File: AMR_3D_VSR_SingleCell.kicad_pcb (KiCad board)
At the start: 2 copper layers, 270.1 x 125 mm, 85 parts, among them P1 CONN_01X01, P2 CONN_01X01, P3 CONN_02X15, P4 CONN_02X05, P5 CONN_02X02, U1 AFF755b, U10 AFF755b, U11 AFF755b, U12 AFF755b, U13 AFF755b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

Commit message: New PCB Layout included, Routing of the signal channesl done.  Committer: Schmitz <ltu@basisit.de>  Changes to be committed: 	modified:   AMR_3D_VSR_SingleCell.kicad_pcb 	modified:   AMR_3D_VSR_SingleCell.kicad_pcb-bak 	modified:   drawing2.dxf
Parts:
- removed the REF** at (144.7, 126.7)
- removed the REF** at (273.7, 145.1)
- moved REF** 338.4 mm to (68.6, -115.7)
- moved REF** 329.0 mm to (80.5, -113.9)
- moved REF** 328.7 mm to (178.2, -113.5)
- moved REF** 324.5 mm to (90.2, -116.8)
- moved REF** 322.2 mm to (123.0, -112.0)
- moved REF** 321.7 mm to (106.7, -119.9)
- moved REF** 317.7 mm to (145.7, -108.9)
- moved REF** 316.1 mm to (126.4, -121.4)
- moved REF** 314.3 mm to (135.2, -119.6)
- moved REF** 314.2 mm to (118.9, -118.8)
- moved REF** 313.8 mm to (152.7, -117.4)
- moved REF** 307.3 mm to (167.5, -111.8)
- moved REF** 296.1 mm to (267.8, -163.1)
- moved REF** 276.5 mm to (277.7, -186.0)
- moved REF** 275.4 mm to (270.2, -176.8)
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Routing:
- net LP-: track 1270.5 -> 0.00 mm, vias 35 -> 0
- net LP+: track 476.5 -> 0.00 mm, vias 19 -> 0
- net +12V: track 148.1 -> 0.00 mm
- net +6V: track 147.6 -> 0.00 mm, vias 6 -> 0
- net U12-: track 120.9 -> 66.0 mm
- net U12+: track 109.8 -> 55.5 mm
- net U15+: track 138.6 -> 85.3 mm
- net Net-(U10-Pad3): track 52.7 -> 0.00 mm
- net Net-(U10-Pad1): track 52.7 -> 0.00 mm
- net U15-: track 145.2 -> 95.4 mm
- net Net-(U5-Pad8): track 45.9 -> 0.00 mm
- net Net-(U5-Pad7): track 40.9 -> 0.00 mm
- net U14+: track 134.9 -> 94.7 mm
- net U14-: track 141.7 -> 105.0 mm
- net Net-(U10-Pad7): track 33.7 -> 0.00 mm, vias 2 -> 0
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- removed copper zone on B.Cu, net LP2-
- removed copper zone on F.Cu, net LP2-
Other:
- board size 270.1 x 125 mm -> 200.8 x 132.1 mm

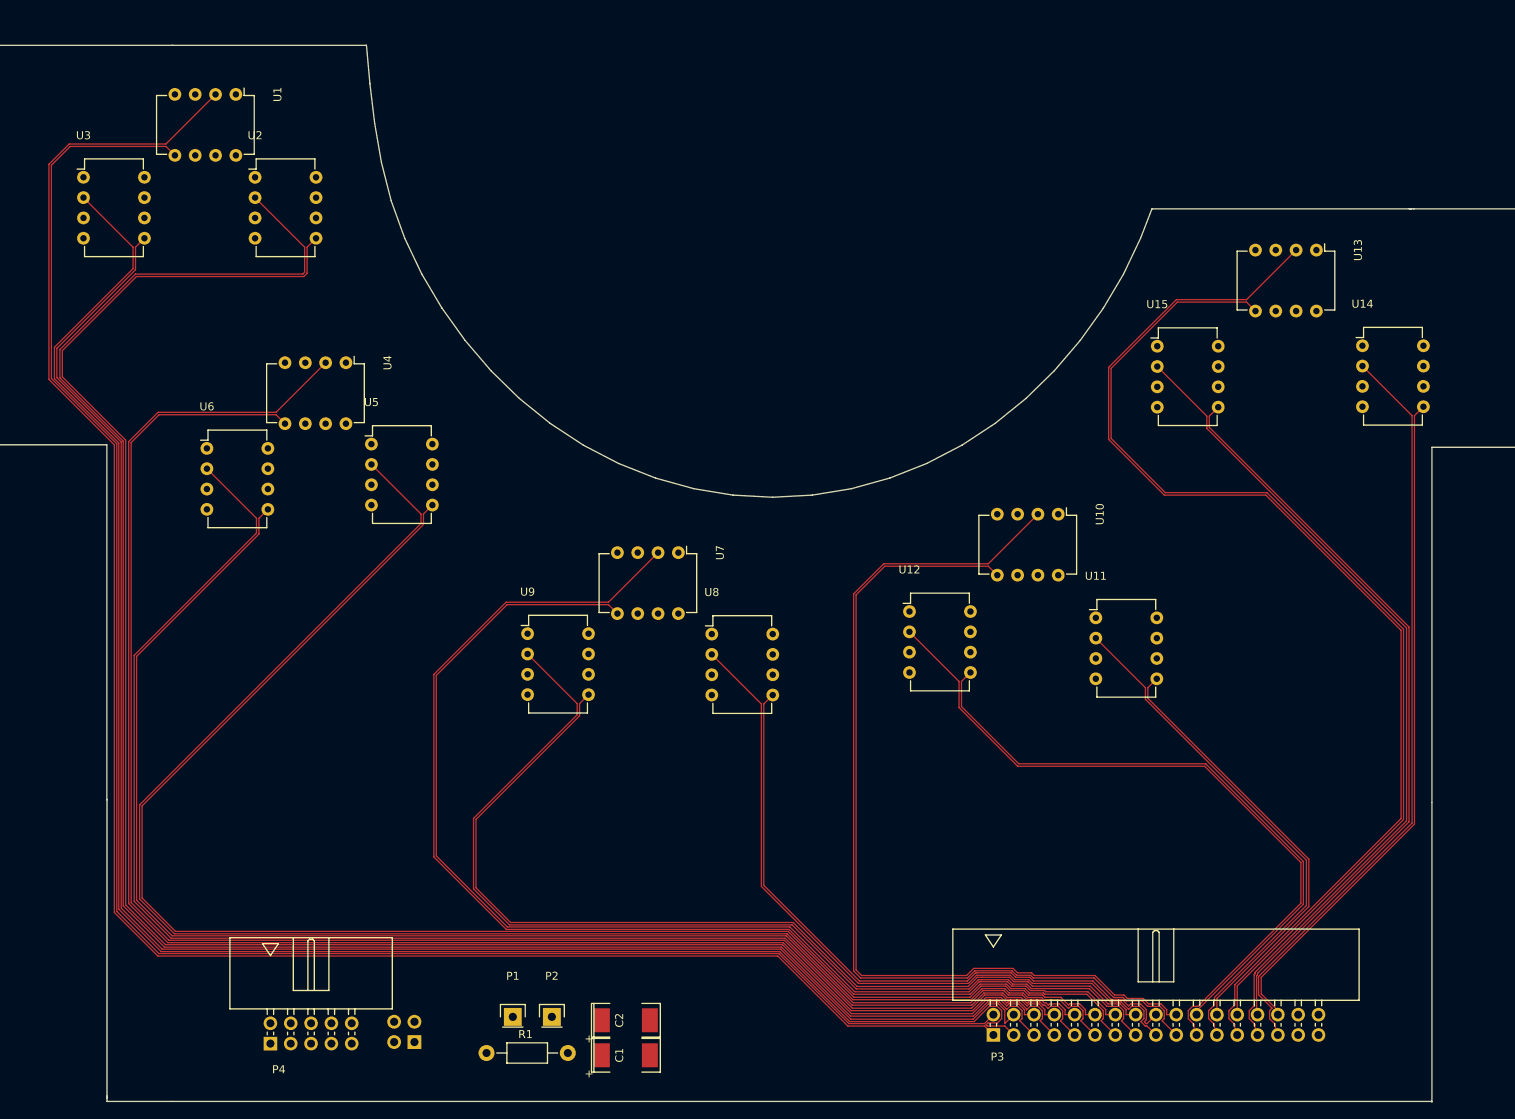
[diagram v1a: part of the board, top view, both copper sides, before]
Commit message: Testspulen verdrahtet.  Committer: Schmitz <ltu@basisit.de>  Changes to be committed: 	modified:   AMR_3D_VSR_SingleCell.kicad_pcb 	modified:   AMR_3D_VSR_SingleCell.kicad_pcb-bak
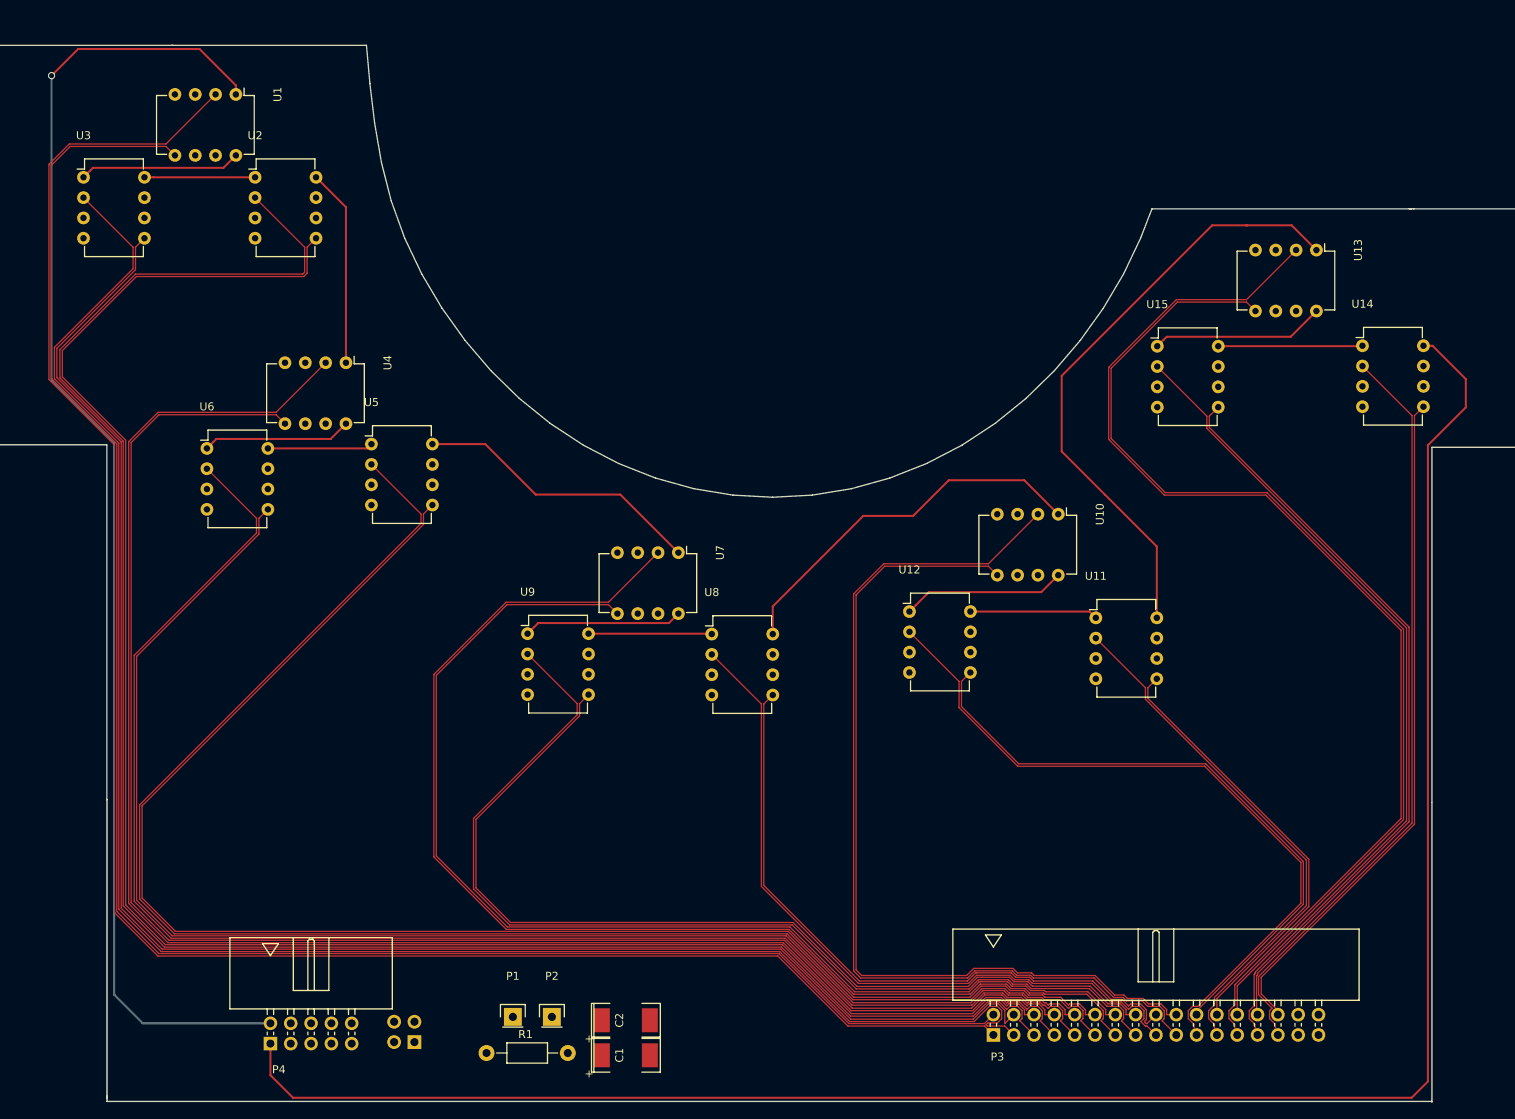
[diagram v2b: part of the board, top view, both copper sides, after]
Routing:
- net LP-: track 0.00 -> 247.4 mm
- net +12V: track 0.00 -> 166.6 mm, vias 0 -> 1
- net Net-(U11-Pad8): track 0.00 -> 76.3 mm
- net Net-(U10-Pad1): track 0.00 -> 47.4 mm
- net Net-(U5-Pad8): track 0.00 -> 36.4 mm
- net Net-(U2-Pad8): track 0.00 -> 24.7 mm
- net Net-(U13-Pad8): track 0.00 -> 21.7 mm
- net Net-(U10-Pad8): track 0.00 -> 20.5 mm
- net Net-(U1-Pad8): track 0.00 -> 20.2 mm
- net Net-(U7-Pad8): track 0.00 -> 19.9 mm
- net Net-(U4-Pad8): track 0.00 -> 18.7 mm
- net Net-(U14-Pad1): track 0.00 -> 18.1 mm
- net Net-(U11-Pad1): track 0.00 -> 16.0 mm
- net Net-(U8-Pad1): track 0.00 -> 15.4 mm
- net Net-(U2-Pad1): track 0.00 -> 13.8 mm
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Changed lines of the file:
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@@
     (thickness 1.6)
     (drawings 58)
-    (tracks 504)
+    (tracks 576)
     (zones 0)
     (modules 83)
@@
     (arrow2b (pts (xy 210.010183 210.239955) (xy 209.42319 209.11375)))
   )
+  (segment (start 131.69222 203.21076) (end 131.69298 203.21) (width 0.254) (layer B.Cu) (net 2))
+  (segment (start 131.69298 203.21) (end 147.65 203.21) (width 0.254) (layer B.Cu) (net 2))
+  (segment (start 128.12606 199.6446) (end 131.69222 203.21076) (width 0.254) (layer B.Cu) (net 2))
+  (segment (start 128.12606 130.71916) (end 128.12606 199.6446) (width 0.254) (layer B.Cu) (net 2))
+  (segment (start 120.29016 122.88326) (end 128.12606 130.71916) (width 0.254) (layer B.Cu) (net 2))
+  (segment (start 120.29016 84.75024) (end 120.29016 122.88326) (width 0.254) (layer B.Cu) (net 2))
+  (segment (start 138.78675 81.42538) (end 123.61502 81.42538) (width 0.254) (layer F.Cu) (net 2))
+  (segment (start 123.61502 81.42538) (end 120.29016 84.75024) (width 0.254) (layer F.Cu) (net 2))
+  (via (at 120.29016 84.75024) (size 0.889) (drill 0.635) (layers F.Cu B.Cu) (net 2))
+  (segment (start 143.33 87.1) (end 143.33 85.96863) (width 0.254) (layer F.Cu) (net 2))
+  (segment (start 143.33 85.96863) (end 138.78675 81.42538) (width 0.254) (layer F.Cu) (net 2))
+  (segment (start 143.33 94.72) (end 141.771001 96.278999) (width 0.254) (layer F.Cu) (net 5))
+  (segment (start 141.771001 96.278999) (end 125.461001 96.278999) (width 0.254) (layer F.Cu) (net 5))
+  (segment (start 125.461001 96.278999) (end 125.079999 96.660001) (width 0.254) (layer F.Cu) (net 5))
+  (segment (start 125.079999 96.660001) (end 124.28 97.46) (width 0.254) (layer F.Cu) (net 5))
+  (segment (start 153.35 97.46) (end 157.09 101.2) (width 0.254) (layer F.Cu) (net 7))
+  (segment (start 157.09 101.2) (end 157.09 120.64) (width 0.254) (layer F.Cu) (net 7))
+  (segment (start 157.09 128.26) (end 155.181001 130.168999) (width 0.254) (layer F.Cu) (net 9))
+  (segment (start 155.181001 130.168999) (end 140.891001 130.168999) (width 0.254) (layer F.Cu) (net 9))
+  (segment (start 140.891001 130.168999) (end 140.509999 130.550001) (width 0.254) (layer F.Cu) (net 9))
+  (segment (start 140.509999 130.550001) (end 139.71 131.35) (width 0.254) (layer F.Cu) (net 9))
+  (segment (start 180.81328 137.11996) (end 191.38396 137.11996) (width 0.254) (layer F.Cu) (net 11))
+  (segment (start 191.38396 137.11996) (end 198.643 144.379) (width 0.254) (layer F.Cu) (net 11))
+  (segment (start 174.50392 130.8106) (end 180.81328 137.11996) (width 0.254) (layer F.Cu) (net 11))
+  (segment (start 167.89484 130.8106) (end 174.50392 130.8106) (width 0.254) (layer F.Cu) (net 11))
+  (segment (start 198.643 151.999) (end 197.461999 153.180001) (width 0.254) (layer F.Cu) (net 13))
+  (segment (start 197.461999 153.180001) (end 181.121999 153.180001) (width 0.254) (layer F.Cu) (net 13))
+  (segment (start 181.121999 153.180001) (end 180.592999 153.709001) (width 0.254) (layer F.Cu) (net 13))
+  (segment (start 180.592999 153.709001) (end 179.793 154.509) (width 0.254) (layer F.Cu) (net 13))
+  (segment (start 232.44132 135.32926) (end 241.8825 135.32926) (width 0.254) (layer F.Cu) (net 15))
+  (segment (start 241.8825 135.32926) (end 246.12684 139.5736) (width 0.254) (layer F.Cu) (net 15))
+  (segment (start 227.98616 139.78442) (end 232.44132 135.32926) (width 0.254) (layer F.Cu) (net 15))
+  (segment (start 221.75808 139.78442) (end 227.98616 139.78442) (width 0.254) (layer F.Cu) (net 15))
+  (segment (start 210.43984 151.10266) (end 221.75808 139.78442) (width 0.254) (layer F.Cu) (net 15))
+  (segment (start 210.43984 154.5596) (end 210.43984 151.10266) (width 0.254) (layer F.Cu) (net 15))
+  (segment (start 246.12684 147.1936) (end 244.00594 149.3145) (width 0.254) (layer F.Cu) (net 17))
+  (segment (start 244.00594 149.3145) (end 229.95466 149.3145) (width 0.254) (layer F.Cu) (net 17))
+  (segment (start 229.95466 149.3145) (end 228.328959 150.940201) (width 0.254) (layer F.Cu) (net 17))
+  (segment (start 228.328959 150.940201) (end 227.52896 151.7402) (width 0.254) (layer F.Cu) (net 17))
+  (segment (start 269.558738 103.46242) (end 269.759 103.46242) (width 0.254) (layer F.Cu) (net 19))
+  (segment (start 269.759 103.46242) (end 275.30128 103.46242) (width 0.254) (layer F.Cu) (net 19))
+  (segment (start 246.5561 122.27874) (end 265.37242 103.46242) (width 0.254) (layer F.Cu) (net 19))
+  (segment (start 265.37242 103.46242) (end 269.759 103.46242) (width 0.254) (layer F.Cu) (net 19))
+  (segment (start 246.5561 131.72246) (end 246.5561 122.27874) (width 0.254) (layer F.Cu) (net 19))
+  (segment (start 251.98497 137.15133) (end 246.5561 131.72246) (width 0.254) (layer F.Cu) (net 19))
+  (segment (start 251.98751 137.15133) (end 251.98497 137.15133) (width 0.254) (layer F.Cu) (net 19))
+  (segment (start 258.44584 152.5276) (end 258.44584 143.60966) (width 0.254) (layer F.Cu) (net 19))
+  (segment (start 258.44584 143.60966) (end 251.98751 137.15133) (width 0.254) (layer F.Cu) (net 19))
+  (segment (start 275.30128 103.46242) (end 278.39754 106.55868) (width 0.254) (layer F.Cu) (net 19))
+  (segment (start 278.39754 114.17868) (end 275.184341 117.391879) (width 0.254) (layer F.Cu) (net 21))
+  (segment (start 275.184341 117.391879) (end 259.685261 117.391879) (width 0.254) (layer F.Cu) (net 21))
+  (segment (start 259.685261 117.391879) (end 259.304259 117.772881) (width 0.254) (layer F.Cu) (net 21))
+  (segment (start 259.304259 117.772881) (end 258.50426 118.57288) (width 0.254) (layer F.Cu) (net 21))
+  (segment (start 150.47552 212.51986) (end 147.65 209.69434) (width 0.254) (layer F.Cu) (net 23))
+  (segment (start 147.65 209.69434) (end 147.65 205.75) (width 0.254) (layer F.Cu) (net 23))
+  (segment (start 290.29998 212.51986) (end 150.47552 212.51986) (width 0.254) (layer F.Cu) (net 23))
+  (segment (start 292.33452 210.48532) (end 290.29998 212.51986) (width 0.254) (layer F.Cu) (net 23))
+  (segment (start 292.33452 130.96046) (end 292.33452 210.48532) (width 0.254) (layer F.Cu) (net 23))
+  (segment (start 297.07416 126.22082) (end 292.33452 130.96046) (width 0.254) (layer F.Cu) (net 23))
+  (segment (start 297.07416 122.68661) (end 297.07416 126.22082) (width 0.254) (layer F.Cu) (net 23))
+  (segment (start 291.77318 118.517) (end 292.90455 118.517) (width 0.254) (layer F.Cu) (net 23))
+  (segment (start 292.90455 118.517) (end 297.07416 122.68661) (width 0.254) (layer F.Cu) (net 23))
   (segment (start 284.15318 121.057) (end 290.350681 127.254501) (width 0.125) (layer F.Cu) (net 24))
   (segment (start 273.275 203.360502) (end 273.275 204.365) (width 0.125) (layer F.Cu) (net 24))
@@
   (segment (start 135.71 94.72) (end 134.592499 93.602499) (width 0.125) (layer F.Cu) (net 53))
   (segment (start 134.592499 93.602499) (end 122.626367 93.602499) (width 0.125) (layer F.Cu) (net 53))
+  (segment (start 131.9 97.46) (end 133.03137 97.46) (width 0.254) (layer F.Cu) (net 54))
+  (segment (start 133.03137 97.46) (end 145.73 97.46) (width 0.254) (layer F.Cu) (net 54))
+  (segment (start 147.33 131.35) (end 159.73544 131.35) (width 0.254) (layer F.Cu) (net 56))
+  (segment (start 159.73544 131.35) (end 160.27484 130.8106) (width 0.254) (layer F.Cu) (net 56))
+  (segment (start 187.413 154.509) (end 202.76924 154.509) (width 0.254) (layer F.Cu) (net 58))
+  (segment (start 202.76924 154.509) (end 202.81984 154.5596) (width 0.254) (layer F.Cu) (net 58))
+  (segment (start 235.14896 151.7402) (end 250.03844 151.7402) (width 0.254) (layer F.Cu) (net 60))
+  (segment (start 250.03844 151.7402) (end 250.82584 152.5276) (width 0.254) (layer F.Cu) (net 60))
+  (segment (start 266.12426 118.57288) (end 284.0973 118.57288) (width 0.254) (layer F.Cu) (net 62))
+  (segment (start 284.0973 118.57288) (end 284.15318 118.517) (width 0.254) (layer F.Cu) (net 62))
   (zone (net 0) (net_name "") (layer B.Cu) (hatch full 0.508)
     (connect_pads (clearance 0.508))

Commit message: Filling of the Cu Plane fixed.  Committer: Schmitz <ltu@basisit.de>  Changes to be committed: 	modified:   AMR_3D_VSR_SingleCell.kicad_pcb 	modified:   AMR_3D_VSR_SingleCell.kicad_pcb-bak
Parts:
- removed R1: R, Resistors_ThroughHole:Resistor_Horizontal_RM10mm
- removed the REF** at (80.5, -113.9)
- removed the REF** at (177.7, -77.5)
- removed the REF** at (184.3, -80.6)
- removed the REF** at (241.2, -62.3)
- removed the REF** at (118.9, -118.8)
- removed the REF** at (276.1, -127.8)
- removed the REF** at (271.8, -138.4)
- removed the REF** at (231.4, -72.7)
- removed the REF** at (106.7, -119.9)
- removed the REF** at (232.6, -50.1)
- removed the REF** at (194.3, -29.9)
- removed the REF** at (153.1, -30.4)
- removed the REF** at (234.0, -57.4)
- removed the REF** at (227.5, -61.7)
- removed the REF** at (142.7, -29.5)
- removed the REF** at (165.5, -31.5)
- removed the REF** at (179.5, -91.5)
- removed the REF** at (219.4, -41.3)
- removed the REF** at (178.0, -28.2)
- removed the REF** at (90.2, -116.8)
- removed the REF** at (167.5, -111.8)
- removed the REF** at (185.2, -49.9)
- removed the REF** at (123.0, -112.0)
- removed the REF** at (275.8, -170.2)
- removed the REF** at (178.2, -113.5)
- removed the REF** at (290.2, -179.6)
- removed the REF** at (289.2, -123.4)
- removed the REF** at (277.7, -186.0)
- removed the REF** at (272.6, -155.6)
- removed the REF** at (268.6, -122.4)
- removed the REF** at (271.1, -92.8)
- removed the REF** at (279.7, -117.3)
- removed the REF** at (267.8, -163.1)
- removed the REF** at (273.9, -144.6)
- removed the REF** at (268.8, -129.1)
- removed the REF** at (176.3, -86.0)
- removed the REF** at (145.7, -108.9)
- removed the REF** at (135.2, -119.6)
- removed the REF** at (112.5, -29.5)
- removed the REF** at (120.9, -34.3)
- removed the REF** at (152.7, -117.4)
- removed the REF** at (172.5, -91.1)
- removed the REF** at (126.4, -121.4)
- removed the REF** at (270.2, -176.8)
- removed the REF** at (68.6, -115.7)
- removed the REF** at (241.2, -39.2)
- removed the REF** at (94.6, -33.4)
- removed the REF** at (97.2, -40.0)
- removed the REF** at (253.3, -20.8)
- removed the REF** at (184.6, -86.5)
- removed the REF** at (229.3, -39.6)
- removed the REF** at (221.5, -32.5)
- removed the REF** at (285.5, -147.6)
- removed the REF** at (256.5, -37.9)
- removed the REF** at (282.7, -171.5)
- removed the REF** at (282.7, -158.8)
- removed the REF** at (286.2, -134.8)
- added REF**: through hole, Connect:1pin, F.Cu at (185.0, 158.3)
- added REF**: through hole, Connect:1pin, F.Cu at (144.7, 133.6)
- added REF**: through hole, Connect:1pin, F.Cu at (201.7, 153.0)
- added REF**: through hole, Connect:1pin, F.Cu at (293.1, 106.3)
- added REF**: through hole, Connect:1pin, F.Cu at (295.4, 124.4)
- added REF**: through hole, Connect:1pin, F.Cu at (265.1, 114.7)
- moved REF** 177.6 mm to (129.8, 100.7)
- moved REF** 169.2 mm to (215.3, 144.0)
- moved REF** 150.2 mm to (262.6, 120.7)
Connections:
- P4 pad 3: LP- -> LP2-
- P4 pad 5: LP2- -> LP-
- REF** pad 1: LP2- -> LP- (x3)
- U14 pad 7: LP- -> LP2-
- U2 pad 6: LP -> LP+
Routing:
- net LP+: track 0.00 -> 380.4 mm, vias 0 -> 1
- net LP2-: track 0.00 -> 244.9 mm
- net +6V: track 0.00 -> 170.4 mm, vias 0 -> 1
- net Net-(U11-Pad7): track 0.00 -> 74.4 mm
- net LP-: track 247.4 -> 297.2 mm
- net Net-(U10-Pad3): track 0.00 -> 48.1 mm
- net Net-(U7-Pad7): track 0.00 -> 41.4 mm
- net Net-(U1-Pad7): track 0.00 -> 37.3 mm
- net Net-(U5-Pad7): track 0.00 -> 34.5 mm
- net Net-(U13-Pad7): track 0.00 -> 29.0 mm
- net Net-(U2-Pad7): track 0.00 -> 26.7 mm
- net +9V: track 0.00 -> 26.5 mm
- net Net-(U10-Pad7): track 0.00 -> 25.7 mm
- net Net-(U4-Pad7): track 0.00 -> 23.9 mm
- net Net-(U14-Pad3): track 0.00 -> 20.7 mm
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- added copper zone on B.Cu, net LP-
- added copper zone on F.Cu, net LP-

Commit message: HZB Logo added to library and to the PCB.  Committer: Schmitz <ltu@basisit.de>  Changes to be committed: 	modified:   AMR_3D_VSR_SingleCell.kicad_pcb 	modified:   AMR_3D_VSR_SingleCell.kicad_pcb-bak 	modified:   AMR_3D_VSR_SingleCell.pro
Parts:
- added G***: LOGO, hzblogo:logo, F.Cu at (283.8, 167.1)
- moved REF** 82.1 mm to (123.5, 128.1)
- moved REF** 8.43 mm to (207.0, 142.4)
- moved REF** 1.08 mm to (143.6, 133.8)
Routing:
- net Net-(U7-Pad7): track 41.4 -> 29.9 mm
- net Net-(U1-Pad7): track 37.3 -> 29.0 mm
- net Net-(U5-Pad1): track 13.2 -> 20.3 mm
- net Net-(U8-Pad1): track 15.4 -> 22.1 mm
- net Net-(U14-Pad1): track 18.1 -> 24.4 mm
- net +12V: track 167.2 -> 171.5 mm
- net +6V: track 170.4 -> 174.6 mm
- net Net-(U1-Pad8): track 20.2 -> 23.0 mm
- net Net-(U5-Pad8): track 36.4 -> 38.5 mm
- net Net-(U2-Pad1): track 13.8 -> 15.5 mm
- net Net-(U14-Pad3): track 20.7 -> 19.1 mm
- net Net-(U13-Pad7): track 29.0 -> 27.4 mm
- net Net-(U10-Pad3): track 48.1 -> 49.4 mm
- net Net-(U5-Pad3): track 15.5 -> 14.4 mm
- net Net-(U8-Pad3): track 17.1 -> 16.5 mm
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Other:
- board text added: "VSR Singlecell B-Board"
